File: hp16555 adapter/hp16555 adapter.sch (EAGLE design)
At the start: 50 parts

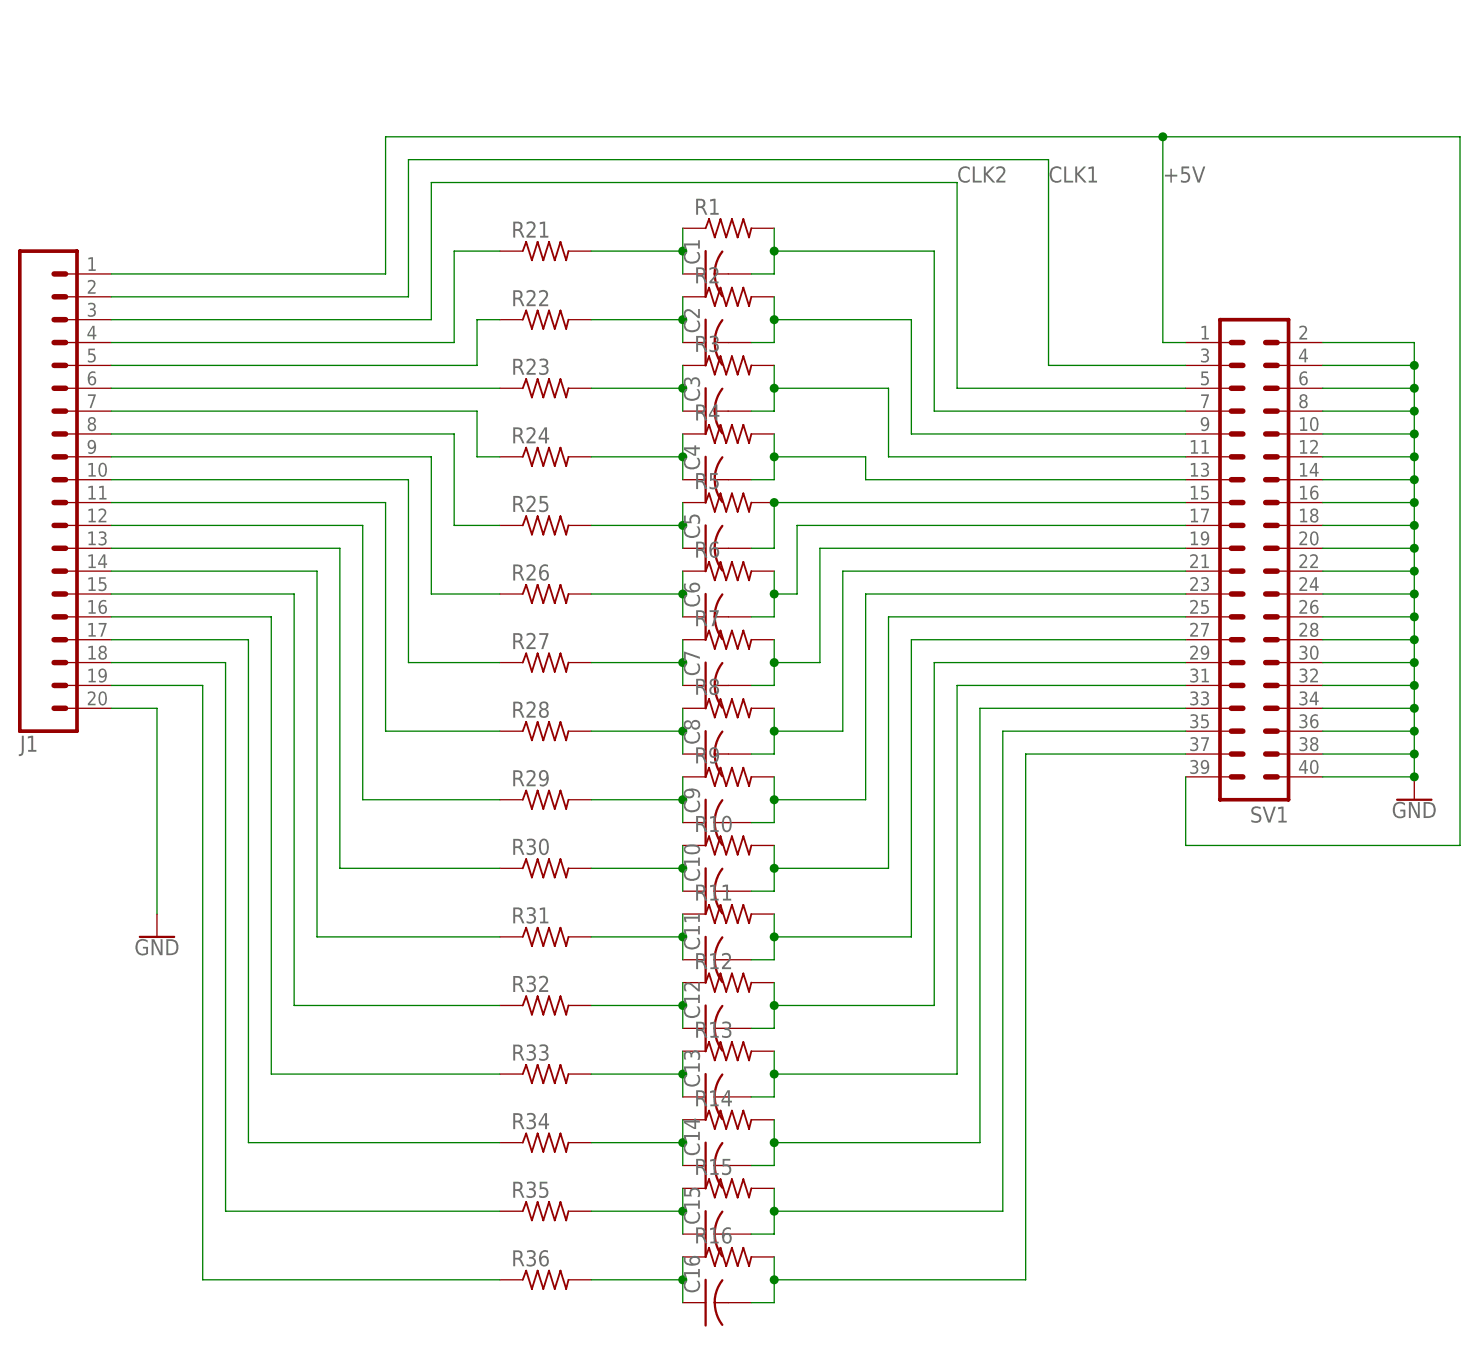
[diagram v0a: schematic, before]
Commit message: Cleaned up design, made it more compact, entered values into schematic
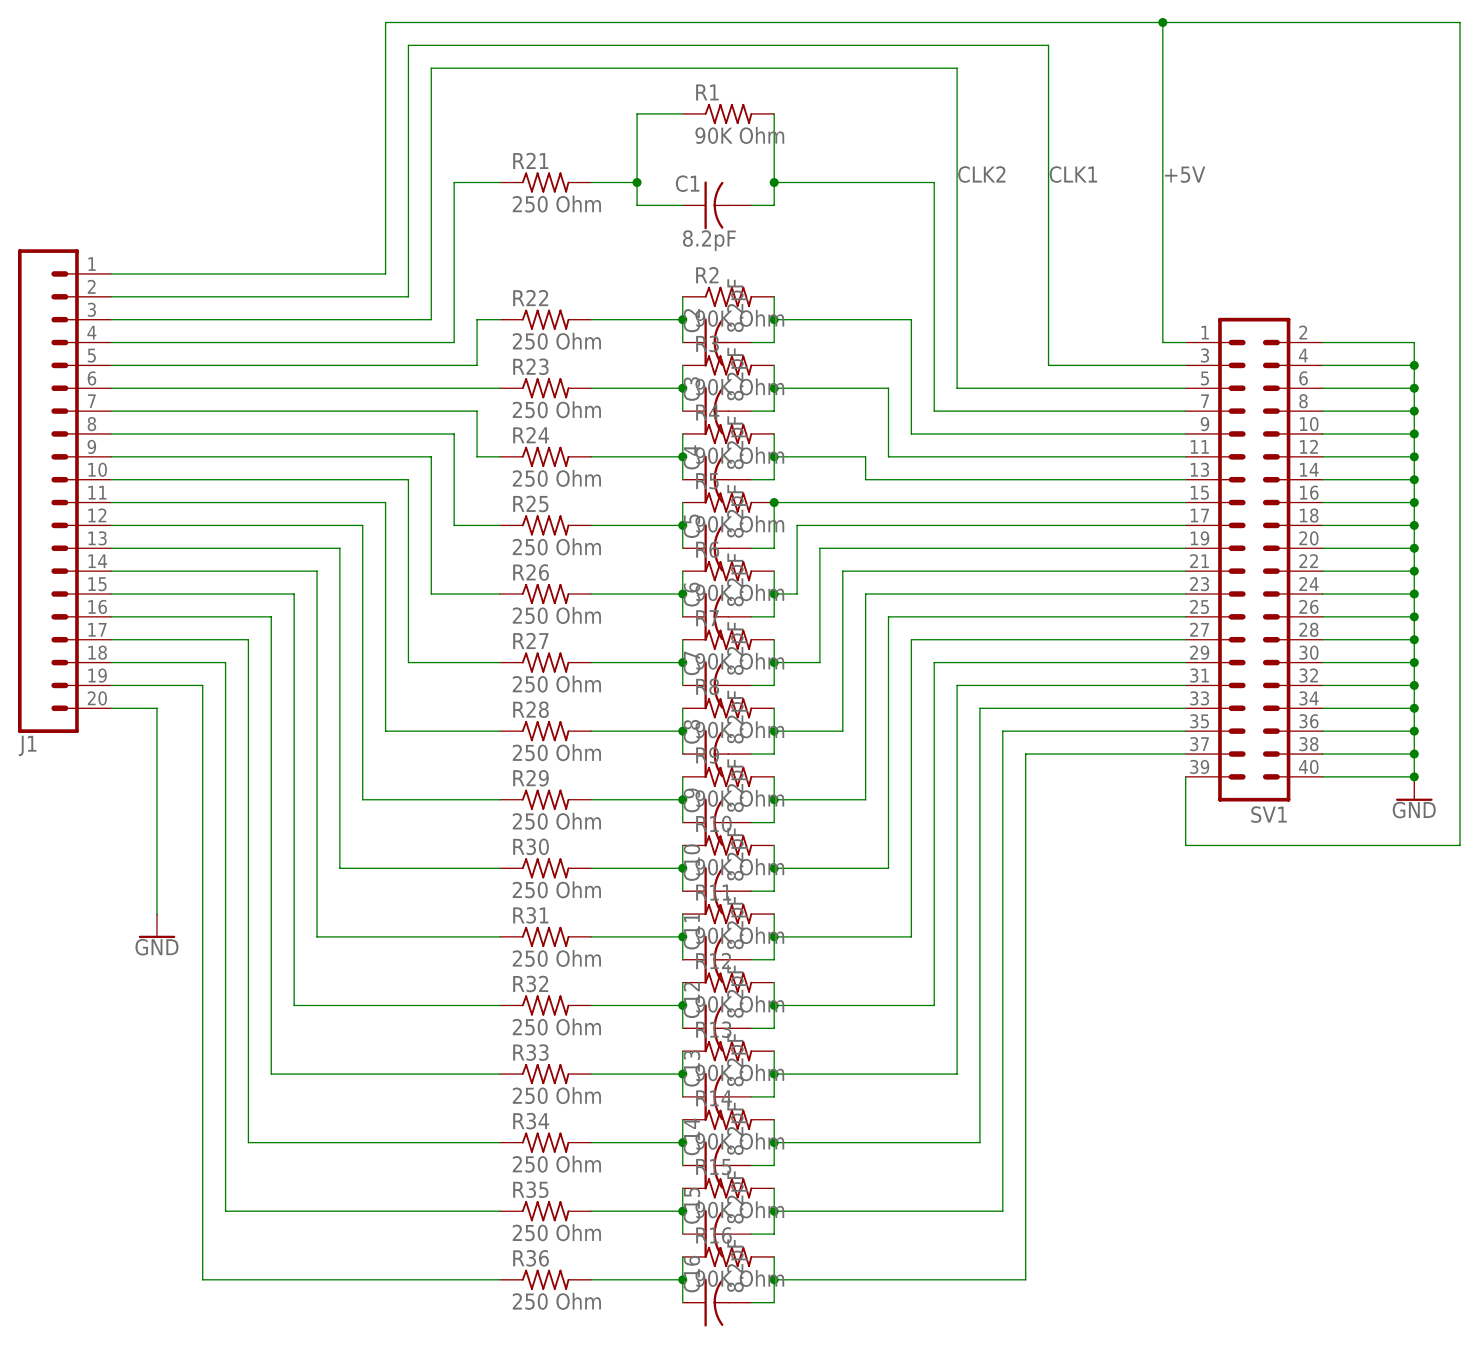
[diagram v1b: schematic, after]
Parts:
- C1, C10, C11, C12, C13, C14, C15, C16, C2, C3, C4, C5, C6, C7, C8, C9: value (none) -> 8.2pF
- R1, R10, R11, R12, R13, R14, R15, R16, R2, R3, R4, R5, R6, R7, R8, R9: value (none) -> 90K Ohm
- R21, R22, R23, R24, R25, R26, R27, R28, R29, R30, R31, R32, R33, R34, R35, R36: value (none) -> 250 Ohm
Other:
- moved on the sheet: C1, R1, R21
